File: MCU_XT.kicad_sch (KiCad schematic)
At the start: 31 parts, among them J10 SWD, J11 UART, J12 I2C1, Q16 AO3401A, Q17 2N7002W, U12 STM32F030C8Tx

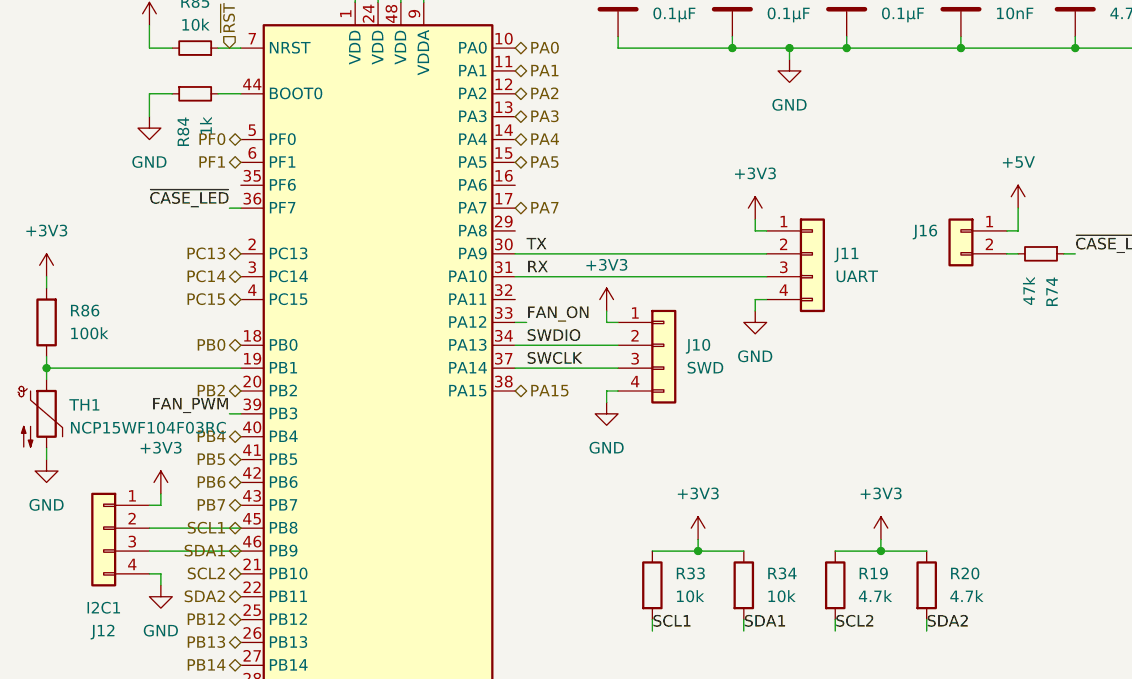
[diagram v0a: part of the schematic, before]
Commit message: fixed wrong net classes
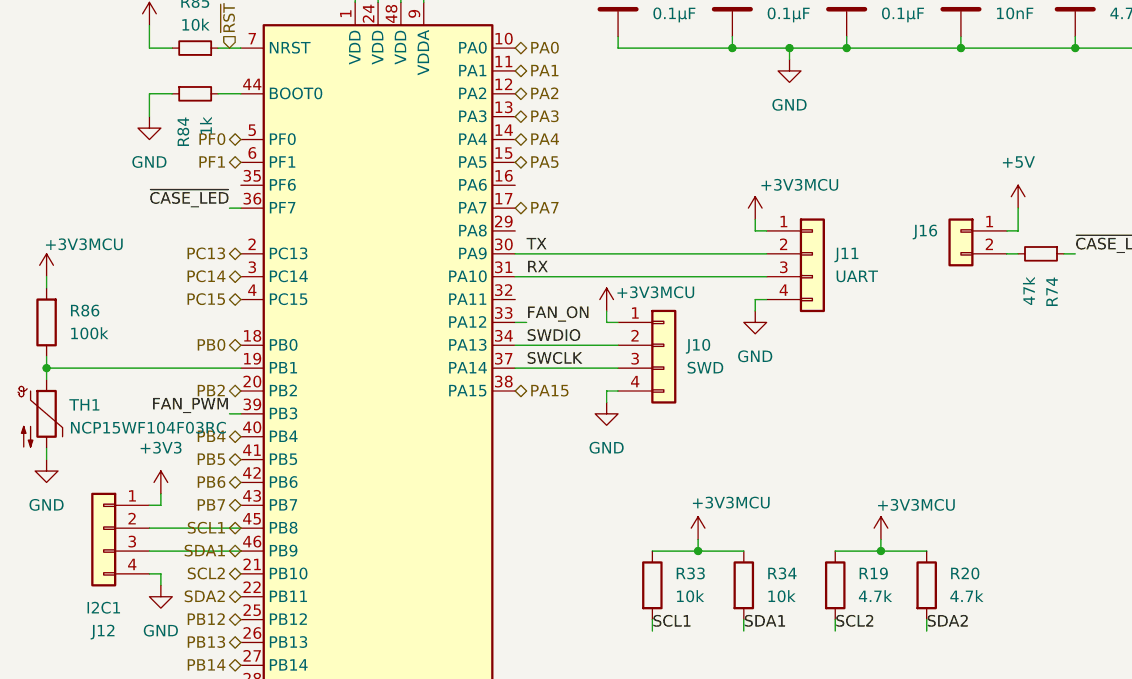
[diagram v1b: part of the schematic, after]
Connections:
- net +3V3: no longer J10.1 (Pin_1), J11.1 (Pin_1), R19.1, R20.1, R33.1, R34.1, R86.2
- net +3V3MCU: now also J10.1 (Pin_1), J11.1 (Pin_1), R19.1, R20.1, R33.1, R34.1, R86.2
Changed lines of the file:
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@@
 		(on_board yes)
 		(dnp no)
-		(fields_autoplaced yes)
 		(property "Reference" "#PWR0125"
 			(at 81.28 73.66 0)
@@
 			)
 		)
-		(property "Value" "+3V3"
-			(at 81.28 64.77 0)
+		(property "Value" "+3V3MCU"
+			(at 82.296 67.818 0)
 			(effects
 				(font
 					(size 1.27 1.27)
 				)
+				(justify left)
 			)
 		)
@@
 		(on_board yes)
 		(dnp no)
-		(fields_autoplaced yes)
 		(property "Reference" "#PWR0128"
 			(at 111.76 99.06 0)
@@
 			)
 		)
-		(property "Value" "+3V3"
-			(at 111.76 90.17 0)
+		(property "Value" "+3V3MCU"
+			(at 111.252 91.44 0)
 			(effects
 				(font
 					(size 1.27 1.27)
 				)
+				(justify left)
 			)
 		)
@@
 		(on_board yes)
 		(dnp no)
-		(fields_autoplaced yes)
 		(property "Reference" "#PWR067"
 			(at 91.44 99.06 0)
@@
 			)
 		)
-		(property "Value" "+3V3"
-			(at 91.44 90.17 0)
+		(property "Value" "+3V3MCU"
+			(at 90.678 91.186 0)
 			(effects
 				(font
 					(size 1.27 1.27)
 				)
+				(justify left)
 			)
 		)
@@
 		(on_board yes)
 		(dnp no)
-		(fields_autoplaced yes)
 		(property "Reference" "#PWR01"
 			(at 97.79 63.5 0)
@@
 			)
 		)
-		(property "Value" "+3V3"
-			(at 97.79 54.61 0)
+		(property "Value" "+3V3MCU"
+			(at 98.298 55.88 0)
 			(effects
 				(font
 					(size 1.27 1.27)
 				)
+				(justify left)
 			)
 		)
@@
 		(on_board yes)
 		(dnp no)
-		(fields_autoplaced yes)
 		(property "Reference" "#PWR068"
 			(at 19.05 69.85 0)
@@
 			)
 		)
-		(property "Value" "+3V3"
-			(at 19.05 60.96 0)
+		(property "Value" "+3V3MCU"
+			(at 18.796 62.484 0)
 			(effects
 				(font
 					(size 1.27 1.27)
 				)
+				(justify left)
 			)
 		)
